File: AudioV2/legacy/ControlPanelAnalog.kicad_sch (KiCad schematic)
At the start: 23 parts, among them SW402 PWR SW, U402 PT2314-D, U403 BP5293-50 +5V

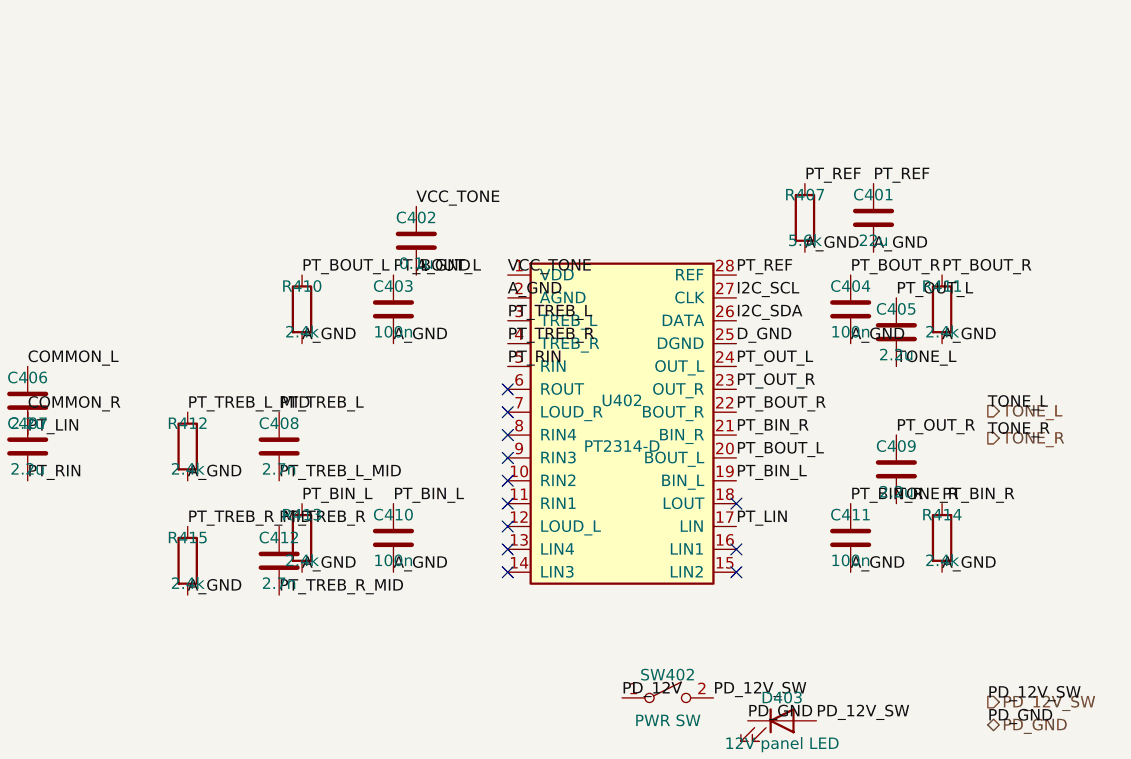
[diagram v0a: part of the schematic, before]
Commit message: AudioV2: PT2314E に切り替え、トーン網をデータシート通りに組み直した
無印 PT2314 は DigiKey に在庫が無く（フォーラムでモデレータ自身が調達困難と
回答し TDA7440 を代替に挙げている）、LCSC / JLCPCB にあるのは PT2314E のみ。
E は "Improved and replace PT2314 and PT2314A" と明記され、28ピンの名前・番号は
無印と完全一致（I2C の 26/27 が DATA/CLK -> SDA/SCL に改名されただけ）。

切り替えにあたって外付け網をデータシートと突き合わせたところ、3箇所ずれていた。
値の一覧は合っていたが置き場所が入れ替わっていた。2.4k は本来「使わないセレクタ
入力の直列抵抗」、5.6k は「低音網の集約点」。

  低音  DS: BOUT -[100n]-+-[5.6k]- GND
                BIN  -[100n]-+          （1点に集約）
        旧: BOUT/BIN が各自 100n と 2.4k で別々に GND。集約点が無く
            BIN->BASS->BOUT の外付け帰還路が成立していなかった
  高音  DS: TREB -[2.7n]- GND
        旧: TREB -[2.7n]-[2.4k]- GND（直列抵抗が余分）
  REF   DS: REF -[22u]- GND
        旧: REF -[22u]- GND に加えて 5.6k で GND へ（内部基準を引いていた）

無印 PT2314 のアプリケーション回路も同じ網なので、E への切り替えとは独立の誤り。

素材 legacy/ControlPanelAnalog.kicad_sch を編集して再生成した。この素材は
ワイヤを持たずラベルをピン先へ直置きする方式なので、配線変更はラベルの
張り替えで足りる。prune() は使っていない（このシートでもラベルを浮きと
誤認して落とすため）。消した部品のラベルはピン先座標で特定して消した。

  R410/R411  2.4k -> 5.6k、集約点 PT_BASS_L/R へ移動
  R407/R412/R413/R414/R415  削除
  C403/C410/C404/C411  GND 側を集約点へ
  C408/C412  中間ノードをやめて直接 A_GND へ
  U402 Value  PT2314-D -> PT2314E

フットプリントは設定していない。SOP-28 300mil だが、入手したDS抜粋に外形寸法が
無く SOIC-28W_7.5x17.9 と 7.5x18.7 のどちらか決められない。誤った値を入れると
「未設定」という目印が消えるので B5 で実物を見てから付ける。

検証:
  erc         17 件（変化なし。新規違反なし）
  netlist     部品 369 / 重複 0（抵抗5本減で 374 -> 369）
  dangling    0 本
  check_sexpr 13 ファイル / 問題 0
  roundtrip   6/6 OK
  再生成      2回目でバイト一致

CLAUDE.md の期待値表と NOW.md も更新した。

Co-Authored-By: Claude Opus 5 <noreply@anthropic.com>
Claude-Session: https://claude.ai/code/session_01VCArLcCGbMGgxvWJ5HFJiY
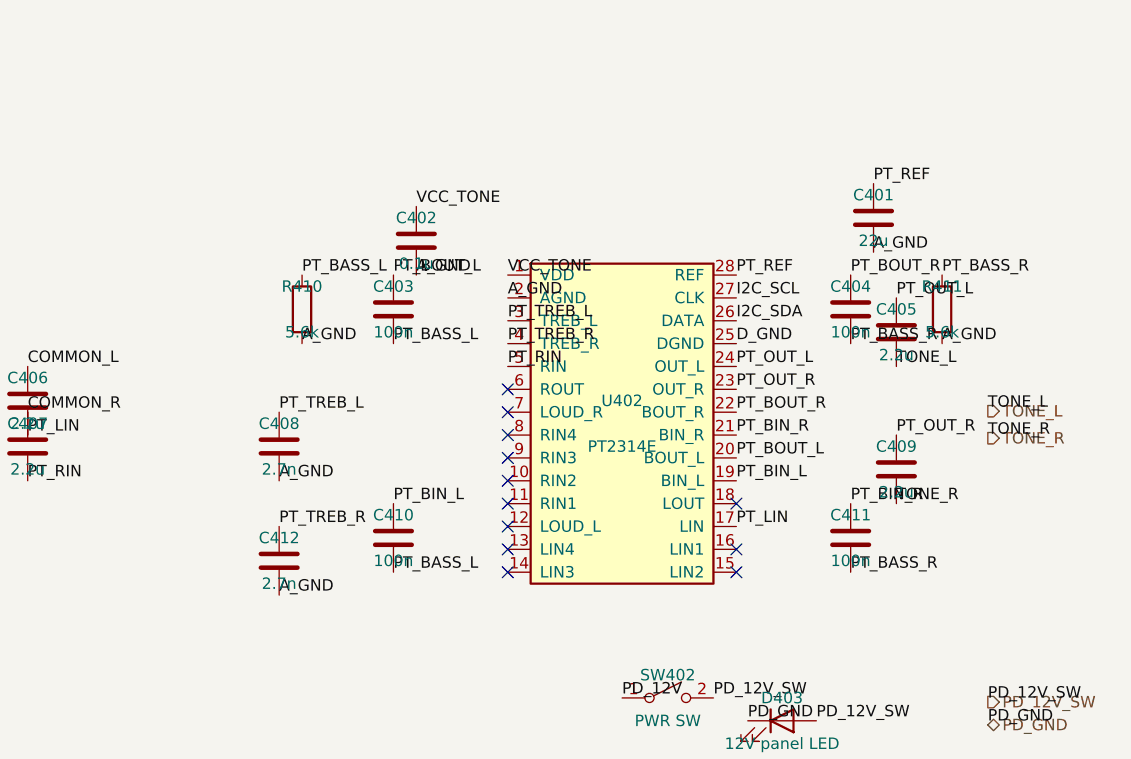
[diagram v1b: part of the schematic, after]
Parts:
- removed R407: 5.6k, symbol Device:R
- removed R412, R413, R414, R415: 2.4k, symbol Device:R
- R410, R411: value 2.4k -> 5.6k
- U402: value PT2314-D -> PT2314E
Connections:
- net PT_TREB_L_MID is gone; now on net A_GND: C408.2
- net PT_TREB_R_MID is gone; now on net A_GND: C412.2
- net A_GND: no longer C403.2, C404.2, C410.2, C411.2
- net PT_BOUT_L: no longer R410.1
- net PT_BOUT_R: no longer R411.1
- new net PT_BASS_L: C403.2, C410.2, R410.1
- new net PT_BASS_R: C404.2, C411.2, R411.1

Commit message: AudioV2: U402 のフットプリントを SOIC-28W_7.5x17.9mm に設定した
JLCPCB の Footprint Manager が出す LCSC の型は
SOP-28_L17.9-W7.5-P1.27-LS10.3 で、外形 17.9 x 7.5・ピッチ 1.27。
KiCad の Package_SO:SOIC-28W_7.5x17.9mm_P1.27mm と一致する。

パッドの伸ばし方だけ違うが、どちらもリードスパン 10.3mm を覆う:

            パッド中心間   パッド寸法      覆う範囲(x)
  LCSC      9.915          0.630 x 1.615   4.150 .. 5.765
  KiCad     9.300          0.600 x 2.050   3.625 .. 5.675
  リード足                                 約 4.35 .. 5.15

KiCad 側は IPC-7351 準拠でヒール側が広い。実装性はどちらでも問題ない。

フットプリント未設定は 45 -> 39。内訳は U402 を設定したぶん 1 個と、
前のコミットで消した抵抗 5 本（R407/R412/R413/R414/R415）がいずれも
未設定組だったぶん。

検証:
  erc         17 件（変化なし）
  netlist     部品 369 / 重複 0（変化なし）
  check_sexpr 13 ファイル / 問題 0
  roundtrip   6/6 OK

Co-Authored-By: Claude Opus 5 <noreply@anthropic.com>
Claude-Session: https://claude.ai/code/session_01VCArLcCGbMGgxvWJ5HFJiY
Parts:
- U402: footprint (none) -> Package_SO:SOIC-28W_7.5x17.9mm_P1.27mm
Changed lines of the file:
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@@
 			)
 		)
-		(property "Footprint" ""
+		(property "Footprint" "Package_SO:SOIC-28W_7.5x17.9mm_P1.27mm"
 			(at 0 0 0)
 			(hide yes)

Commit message: AudioV2: 母板のフットプリント 23 個を設計内の前例に合わせて埋めた（39 -> 16）
B5 の下ごしらえ。前例のあるものだけを埋め、判断が要るものには触っていない。

  積セラ 1206     C202/204/206/208/402, C403/404/410/411, C408/412
                  設計で 85 回使われている流儀に合わせた
  抵抗 1206       R410/411（同 128 回）
  フィルム        C405/406/407/409（2.2u）
                  PT2314 の入出力結合で音声が通る。設計内の C601「2.2uF film」と
                  同じ footprint に揃えた。セラミックは電圧で容量が変わるので
                  結合位置に置くと歪む（ユーザー判断 2026-09-07）
  電解            C201/205/207(47u) -> D8.0/P3.50（C1610・C1621 と同じ）
                  C401(22u)         -> D6.3/P2.50（C1630 と同じ）
                  C203(10u)         -> D5.0/P2.00（C1635「10uF 50V」と同じ）
  DC-DC           U403 -> Library:BP5293-50_ROHM_SIP-3
                  U1607 が同一部品で同じ footprint

素材（legacy/ControlPanelAnalog 15個・legacy/PowerModule 8個）を編集して再生成した。

**残り 16 個には触っていない。** 性質が2つに分かれる:

  パネル部品 6（RV501/502・SW501/502/1601・SW402）
    KiCad にもプロジェクトの Audio/Library.pretty にも footprint が無い。
    Alps は RK097/RK09K しかなく RK27 は別物。C&K 7000 系トグルも無い。
    データシートから新規に作る作業になる。
    さらに SW501/502/1601 は現物1個の 3PDT を3シンボルで表しているので、
    3つ全部に footprint を入れると PCB にスイッチが3個並ぶ。1個化が要る。

  調達判断待ち 10（D403・F201/202/203・J201/202・J_HP501・J_LINE501・
    J_RAIL501・U202）

検証:
  未設定      39 -> 16
  netlist     部品 370 / 重複 0（変化なし）
  erc         17 件（変化なし）
  check_sexpr 13 ファイル / 問題 0
  roundtrip   6/6 OK
  再生成      2回目でバイト一致

Co-Authored-By: Claude Opus 5 <noreply@anthropic.com>
Claude-Session: https://claude.ai/code/session_01VCArLcCGbMGgxvWJ5HFJiY
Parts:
- C401: footprint (none) -> Capacitor_THT:CP_Radial_D6.3mm_P2.50mm
- C402, C403, C404, C408, C410, C411, C412: footprint (none) -> Capacitor_SMD:C_1206_3216Metric_Pad1.33x1.80mm_HandSolder
- C405, C406, C407, C409: footprint (none) -> Capacitor_THT:C_Rect_L7.2mm_W2.5mm_P5.00mm_FKS2_FKP2_MKS2_MKP2
- R410, R411: footprint (none) -> Resistor_SMD:R_1206_3216Metric_Pad1.30x1.75mm_HandSolder
- U403: footprint (none) -> Library:BP5293-50_ROHM_SIP-3
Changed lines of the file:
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@@
 			)
 		)
-		(property "Footprint" ""
+		(property "Footprint" "Capacitor_SMD:C_1206_3216Metric_Pad1.33x1.80mm_HandSolder"
 			(at 0 0 0)
 			(hide yes)
@@
 			)
 		)
-		(property "Footprint" ""
+		(property "Footprint" "Capacitor_SMD:C_1206_3216Metric_Pad1.33x1.80mm_HandSolder"
 			(at 0 0 0)
 			(hide yes)
@@
 			)
 		)
-		(property "Footprint" ""
+		(property "Footprint" "Capacitor_SMD:C_1206_3216Metric_Pad1.33x1.80mm_HandSolder"
 			(at 0 0 0)
 			(hide yes)
@@
 			)
 		)
-		(property "Footprint" ""
+		(property "Footprint" "Capacitor_SMD:C_1206_3216Metric_Pad1.33x1.80mm_HandSolder"
 			(at 0 0 0)
 			(hide yes)
@@
 			)
 		)
-		(property "Footprint" ""
+		(property "Footprint" "Capacitor_THT:C_Rect_L7.2mm_W2.5mm_P5.00mm_FKS2_FKP2_MKS2_MKP2"
 			(at 0 0 0)
 			(hide yes)
@@
 			)
 		)
-		(property "Footprint" ""
+		(property "Footprint" "Resistor_SMD:R_1206_3216Metric_Pad1.30x1.75mm_HandSolder"
 			(at 0 0 0)
 			(hide yes)
@@
 			)
 		)
-		(property "Footprint" ""
+		(property "Footprint" "Capacitor_SMD:C_1206_3216Metric_Pad1.33x1.80mm_HandSolder"
 			(at 0 0 0)
 			(hide yes)
@@
 			)
 		)
-		(property "Footprint" ""
+		(property "Footprint" "Capacitor_THT:CP_Radial_D6.3mm_P2.50mm"
 			(at 0 0 0)
 			(hide yes)
@@
 			)
 		)
-		(property "Footprint" ""
+		(property "Footprint" "Capacitor_THT:C_Rect_L7.2mm_W2.5mm_P5.00mm_FKS2_FKP2_MKS2_MKP2"
 			(at 0 0 0)
 			(hide yes)
@@
 			)
 		)
-		(property "Footprint" ""
+		(property "Footprint" "Library:BP5293-50_ROHM_SIP-3"
 			(at 0 0 0)
 			(hide yes)
@@
 			)
 		)
-		(property "Footprint" ""
+		(property "Footprint" "Capacitor_SMD:C_1206_3216Metric_Pad1.33x1.80mm_HandSolder"
 			(at 0 0 0)
 			(hide yes)
@@
 			)
 		)
-		(property "Footprint" ""
+		(property "Footprint" "Capacitor_THT:C_Rect_L7.2mm_W2.5mm_P5.00mm_FKS2_FKP2_MKS2_MKP2"
 			(at 0 0 0)
 			(hide yes)
@@
 			)
 		)
-		(property "Footprint" ""
+		(property "Footprint" "Capacitor_THT:C_Rect_L7.2mm_W2.5mm_P5.00mm_FKS2_FKP2_MKS2_MKP2"
 			(at 0 0 0)
 			(hide yes)
@@
 			)
 		)
-		(property "Footprint" ""
+		(property "Footprint" "Capacitor_SMD:C_1206_3216Metric_Pad1.33x1.80mm_HandSolder"
 			(at 0 0 0)
 			(hide yes)
@@
 			)
 		)
-		(property "Footprint" ""
-			(at 0 0 0)
-			(hide yes)
+		(property "Footprint" "Resistor_SMD:R_1206_3216Metric_Pad1.30x1.75mm_HandSolder"
+			(at 0 0 0)
+			(hide yes)

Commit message: AudioV2: パネル部品6個をヘッダのフットプリントにした（16 -> 10）
PARTS.md がヘッダ構成まで既に指定していた。それに従っただけで、新しい判断は
入れていない。

  PARTS.md:5    RV / SW_DEST / ENC / PWR SW は パネル実装。基板はヘッダ＋リード
  PARTS.md:173  RV は基板 6P ヘッダ（Device:R_Potentiometer_Dual ピン番号のまま）
  PARTS.md:141  SW_DEST は 現物端子 -> 基板ヘッダ（音声 2x4 + センス 1x3）

  RV501/502     PinHeader_1x06   シンボルのピン 1-6 がそのままヘッダのピン
  SW501/502     PinHeader_1x04   PARTS.md §2.1 の SW601-1..4 / SW602-1..4 に対応
  SW1601        PinHeader_1x04   同じ並び。pin2(MUTE) は基板側で未使用
  SW402         PinHeader_1x02   SPST

ポットの品種（Alps RK27 か RK097 か Alpha RD901 か）は決めていない。
PARTS.md が「RK097 でも回路は同一」「A50k デュアルならピン互換で可」と
書いており、電気的な要件は A カーブ・50k・2連だけ。**ヘッダなので基板側は
品種に依存しない**。入手性と性能で選ぶ調達判断として残す（ユーザー判断 2026-09-07）。

⚠ PARTS.md の「音声 2x4」は 2行4列ではなく「4ピンを2組」と読んだ。同 §2.1 の
ピン対応表が SW601-1..4 / SW602-1..4 と別々に並べており、シンボルも2つに
分かれているため。2行4列の1個を意図していたなら要修正。

副次的に、Cursor 査読の「DEST の 3PDT が自動 BOM 上で現物3個に見える」も解ける。
基板に載るのはヘッダ3個（実際に3個要る）で、スイッチ本体はパネル部品として
基板 BOM に出ないのが正しい形。

なお PARTS.md §2.1 のピン対応表は SW601-3 をコモン（AMP_SEL_L）としており、
今日 SW1601 で直した割り当て（pin3=コモン）と一致していた。

検証:
  未設定      16 -> 10（残りは D403・F201/202/203・J201/202・J_HP501・
              J_LINE501・J_RAIL501・U202。すべて調達判断待ち）
  netlist     部品 370 / 重複 0（変化なし）
  erc         17 件（変化なし）
  check_sexpr 13 ファイル / 問題 0
  roundtrip   6/6 OK
  再生成      2回目でバイト一致

Co-Authored-By: Claude Opus 5 <noreply@anthropic.com>
Claude-Session: https://claude.ai/code/session_01VCArLcCGbMGgxvWJ5HFJiY
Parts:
- SW402: footprint (none) -> Connector_PinHeader_2.54mm:PinHeader_1x02_P2.54mm_Vertical
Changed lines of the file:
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@@
 			)
 		)
-		(property "Footprint" ""
+		(property "Footprint" "Connector_PinHeader_2.54mm:PinHeader_1x02_P2.54mm_Vertical"
 			(at 0 0 0)
 			(hide yes)

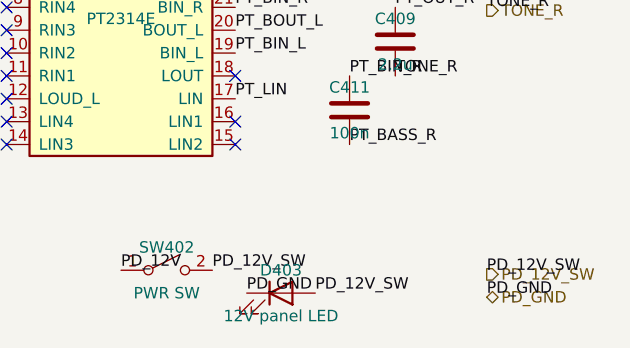
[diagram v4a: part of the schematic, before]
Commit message: AudioV2: 残り5個のフットプリントを埋めた（5 -> 0）。D403 に直列抵抗 R401
フットプリント未設定 0 個。これで netlist 上の 371 部品すべてに footprint が付いた。

- F201/F202/F203 … Resistor_THT:R_Axial_DIN0411_L9.9mm_D3.6mm_P12.70mm_Horizontal
  設計内の F1601/F1602/F1603 と同じリード品に揃えた。ピッチが3種類に散らばる
  より、入手性のいい 5x20mm 相当の軸形1種に寄せたほうが調達が楽になる
- U202 … Package_TO_SOT_THT:TO-220-3_Vertical
  垂直立て。放熱器の要否と向きは PCB を起こすとき（B5）に決め直す
- D403 … LED_THT:LED_D5.0mm（設計内の D1610/D1611 と同じ）

D403 は PD_12V_SW に直付けだったので、電流制限の 2.2k を直列に入れた:

    PD_12V_SW ─[R401 2.2k]─ LED_12V_A ─[D403]─ PD_GND

抵抗なしだと LED の Vf ばらつきがそのまま電流に出る。12V で Vf 2.0V 想定なら
約 4.5mA。部品数 370 -> 371（CLAUDE.md の期待値も更新）。

生成シートは直接触らず、素材の legacy/ControlPanelAnalog.kicad_sch と
legacy/PowerModule.kicad_sch を編集して build_daughter -> build_motherboard で
再生成した。

検証:
  check_sexpr.py -q AudioV2        13 ファイル / 問題 0
  kicad-run.sh erc                 17 件（変化なし）
  kicad-run.sh netlist             部品 371 個・重複 0・footprint 未設定 0
  sch_import.py --roundtrip        6/6 OK
  再生成の冪等性                    バイト一致

⚠ PARTS.md の「音声 2×4」は「4ピンのヘッダを2組」と読んで 2 x PinHeader_1x04 に
した。2行4列（PinHeader_2x04）のつもりだったなら直す必要がある。

Co-Authored-By: Claude Opus 5 <noreply@anthropic.com>
Claude-Session: https://claude.ai/code/session_01VCArLcCGbMGgxvWJ5HFJiY
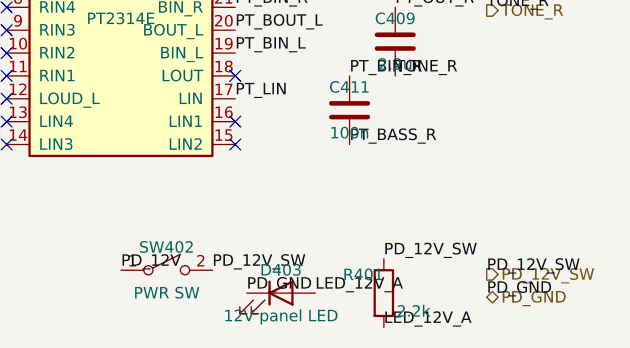
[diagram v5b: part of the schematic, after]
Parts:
- added R401: 2.2k, Resistor_SMD:R_1206_3216Metric_Pad1.30x1.75mm_HandSolder, symbol Device:R
- D403: footprint (none) -> LED_THT:LED_D5.0mm
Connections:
- net PD_12V_SW: now also R401.1; no longer D403.2 (A)
- new net LED_12V_A: D403.2 (A), R401.2
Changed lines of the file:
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@@
 		)
 	)
-	(label "PD_12V_SW"
+	(label "LED_12V_A"
 		(at 181.61 152.4 0)
 		(effects
@@
 			)
 		)
-		(property "Footprint" ""
+		(property "Footprint" "LED_THT:LED_D5.0mm"
 			(at 0 0 0)
 			(hide yes)
@@
 		)
 	)
+	(symbol
+		(lib_id "Device:R")
+		(at 189.23 152.4 0)
+		(unit 1)
+		(body_style 1)
+		(exclude_from_sim no)
+		(in_bom yes)
+		(on_board yes)
+		(in_pos_files yes)
+		(dnp no)
+		(property "Reference" "R401"
+			(at 186.944 150.368 0)
+			(show_name no)
+			(do_not_autoplace no)
+			(effects
+				(font
+					(size 1.27 1.27)
+				)
+			)
+		)
+		(property "Value" "2.2k"
+			(at 192.532 154.432 0)
+			(show_name no)
+			(do_not_autoplace no)
+			(effects
+				(font
+					(size 1.27 1.27)
+				)
+			)
+		)
+		(property "Footprint" "Resistor_SMD:R_1206_3216Metric_Pad1.30x1.75mm_HandSolder"
+			(at 189.23 152.4 0)
+			(hide yes)
+			(show_name no)
+			(do_not_autoplace no)
+			(effects
+				(font
+					(size 1.27 1.27)
+				)
+			)
+		)
+		(property "Datasheet" ""
+			(at 189.23 152.4 0)
+			(hide yes)
+			(show_name no)
+			(do_not_autoplace no)
+			(effects
+				(font
+					(size 1.27 1.27)
+				)
+			)
+		)
+		(property "Description" "D403(12V パネル LED)の直列抵抗。素の LED でも 12V 直結で壊れないようにする。(12-Vf2)/2.2k = 約 4.5mA。抵抗内蔵の 12V LED を挿しても点く（やや暗い）。"
+			(at 189.23 152.4 0)
+			(hide yes)
+			(show_name no)
+			(do_not_autoplace no)
+			(effects
+				(font
+					(size 1.27 1.27)
+				)
+			)
+		)
+		(pin "1"
+		)
+		(pin "2"
+		)
+		(instances
+			(project "AudioV2Case"
+				(path "/a1000001-0001-4001-8001-000000000001/a1000012-0012-4012-8012-000000000012"
+					(reference "R401")
+					(unit 1)
+				)
+			)
+		)
+	)
+	(label "PD_12V_SW"
+		(at 189.23 148.59 0)
+		(effects
+			(font
+				(size 1.27 1.27)
+			)
+			(justify left bottom)
+		)
+	)
+	(label "LED_12V_A"
+		(at 189.23 156.21 0)
+		(effects
+			(font
+				(size 1.27 1.27)
+			)
+			(justify left bottom)
+		)
+	)

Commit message: AudioV2: 外部入力端子台を入れ、ENC の名前と UI の割り込みを直した（ERC 17 -> 11）
査読の確認で出た3件。ERC は 17 -> 11 件になり、残る11件は全部「宣言済みの型」に
収まった（内訳は CLAUDE.md の表）。

1. 外部入力 L/R の端子台 J_IN401 を追加

   DECISIONS §11.3（基板間リンク）は「外部入力 L/R｜端子台 2〜3P」で確定と
   書いてあるのに symbol が無く、COMMON_L / COMMON_R が1ピン（結合Cの片足だけ）
   だった。出力側は J_HP501 / J_LINE501 が実在するのに入力だけ抜けていた。
   このまま PCB を起こすと入力パッドが空かない。

       J_IN401 → COMMON_L →C406→ PT_LIN → PT2314E → PT_OUT_L →C405→ TONE_L → …

   1=L / 2=A_GND / 3=R。L と R の間に必ず GND が挟まる並び。フットプリントは
   J_RAIL501 と同じ Phoenix MKDS-1,5 3P（横）。
   これで isolated_pin_label が 9 -> 1 件になった（残る1件は DEST_SENSE_MUTE_NC で、
   ミュート位置なので意図的に開放）。

2. ENC1602 の Value を ENC_VOL -> ENC_BASS

   確定は CH / BASS / TREBLE（DECISIONS §2「ENC 割当（確定）」・§10 の表・
   CIRCUIT_DESIGN.md）。「音量をエンコーダー化」は 2026-08-30 に撤回済み。
   そもそも PT2314E のボリューム段は LOUT/ROUT -> LIN/RIN のインサートで
   飛ばしているので、VOL のエンコーダには制御対象が無い。

3. U1610（UI 0x22）の INTA(20) / INTB(19) を Pico の GP16 / GP17 へ

   エンコーダ3個が MCP23017 経由なので、割り込みが無いとポーリングしかない。
   I²C は PT2314E の VDD 9V（L7809CV）× MCU 3.3V により Standard 100 kbit/s 止まり
   （DS p.7 の DATA RATE 表）で、2.42″ OLED が 128x64 なら1フレーム 1024 バイト
   ≈ 92 ms。取りこぼさない周期でエンコーダを叩くとバス占有が単独で 45% になり
   同居できない。

   ⚠ 2本引いたのは MIRROR ビット頼みにしないため。ENC1/2 の A/B/SW と ENC3 の A/B は
     PortA(21-28) だが ENC3_SW だけ PortB(pin1) にいるので、INTA だけだと
     IOCON.MIRROR=1 が前提になる。ADC 兼用の GP26-28 は空けたまま。

Pico の AGND(33) は開放のまま戻した（いったん D_GND へ結んだが撤回）

   lib シンボル MCU_Module:RaspberryPi_Pico は pin3 GND と pin33 AGND を
   どちらも power_out と型付けしている（他の GND 6本は passive）。モジュール側が
   それぞれをグランド源として出しているという宣言なので、外で結ぶと power_out
   同士の衝突になり、実際 pin_to_pin エラーが出た。AGND は Pico 基板上で
   グランドに繋がっている前提でよい。

PARTS.md は再生成した（gen_parts_bom.py）

   生成ブロックが 部品総数 368 / Footprint 未設定 44 の時代のまま止まっていたので、
   このセッションで埋めた footprint 全部と R401 / C1645 / F1603 / J_IN401、
   削除した R407・R412-415 が一気に反映された。
   ⚠ U402 の Role にあった「SOP-28 300 mil。LCSC C90034」は 2fbad17 で
     生成ブロックの中を手編集していたもので、再生成で消えた（マーカー内は毎回
     まるごと差し替わるので当然）。回路図側の Description プロパティに入れ直した。
   §5 の「Footprint 未設定の部品」は 0 個になったので残件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
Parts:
- added J_IN401: AUDIO IN L/R, TerminalBlock_Phoenix:TerminalBlock_Phoenix_MKDS-1,5-3-5.08_1x03_P5.08mm_Horizontal, symbol Connector:Screw_Terminal_01x03
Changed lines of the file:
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@@
+	)
+	(symbol
+		(lib_id "Connector:Screw_Terminal_01x03")
+		(at 76.2 118.11 0)
+		(unit 1)
+		(body_style 1)
+		(exclude_from_sim no)
+		(in_bom yes)
+		(on_board yes)
+		(in_pos_files yes)
+		(dnp no)
+		(property "Reference" "J_IN401"
+			(at 76.2 109.22 0)
+			(show_name no)
+			(do_not_autoplace no)
+			(effects
+				(font
+					(size 1.27 1.27)
+				)
+			)
+		)
+		(property "Value" "AUDIO IN L/R"
+			(at 76.2 111.76 0)
+			(show_name no)
+			(do_not_autoplace no)
+			(effects
+				(font
+					(size 1.27 1.27)
+				)
+			)
+		)
+		(property "Footprint" "TerminalBlock_Phoenix:TerminalBlock_Phoenix_MKDS-1,5-3-5.08_1x03_P5.08mm_Horizontal"
+			(at 76.2 118.11 0)
+			(hide yes)
+			(show_name no)
+			(do_not_autoplace no)
+			(effects
+				(font
+					(size 1.27 1.27)
+				)
+			)
+		)
+		(property "Datasheet" ""
+			(at 76.2 118.11 0)
+			(hide yes)
+			(show_name no)
+			(do_not_autoplace no)
+			(effects
+				(font
+					(size 1.27 1.27)
+				)
+			)
+		)
+		(property "Description" "箱の外部音声入力。1=L / 2=A_GND / 3=R。ここから結合C経由で PT2314E の LIN/RIN へ入る（セレクタとボリューム段は LOUT/ROUT->LIN/RIN のインサートで飛ばしている）。L と R の間に GND を挟むため 3P にした。"
+			(at 76.2 118.11 0)
+			(hide yes)
+			(show_name no)
+			(do_not_autoplace no)
+			(effects
+				(font
+					(size 1.27 1.27)
+				)
+			)
+		)
+		(pin "1"
+		)
+		(pin "2"
+		)
+		(pin "3"
+		)
+		(instances
+			(project "AudioV2Case"
+				(path "/a1000001-0001-4001-8001-000000000001/a1000012-0012-4012-8012-000000000012"
+					(reference "J_IN401")
+					(unit 1)
+				)
+			)
+		)
+	)
+	(label "COMMON_L"
+		(at 71.12 115.57 180)
+		(effects
+			(font
+				(size 1.27 1.27)
+			)
+			(justify right bottom)
+		)
+	)
+	(label "A_GND"
+		(at 71.12 118.11 180)
+		(effects
+			(font
+				(size 1.27 1.27)
+			)
+			(justify right bottom)
+		)
+	)
+	(label "COMMON_R"
+		(at 71.12 120.65 180)
+		(effects
+			(font
+				(size 1.27 1.27)
+			)
+			(justify right bottom)
+		)
 	)
 	(symbol
@@
 			)
 		)
-		(property "Description" ""
-			(at 0 0 0)
-			(hide yes)
+		(property "Description" "SOP-28 300 mil（表面実装。無印 PT2314 の DIP 版は入手不可）。LCSC C90034。トーン段だけ使う — 入力セレクタとボリューム段は LOUT/ROUT -> LIN/RIN の インサート点で飛ばしていて、未使用12ピンには no_connect を立ててある。"
+			(at 0 0 0)
+			(hide yes)
